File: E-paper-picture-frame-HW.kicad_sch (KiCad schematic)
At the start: 0 parts

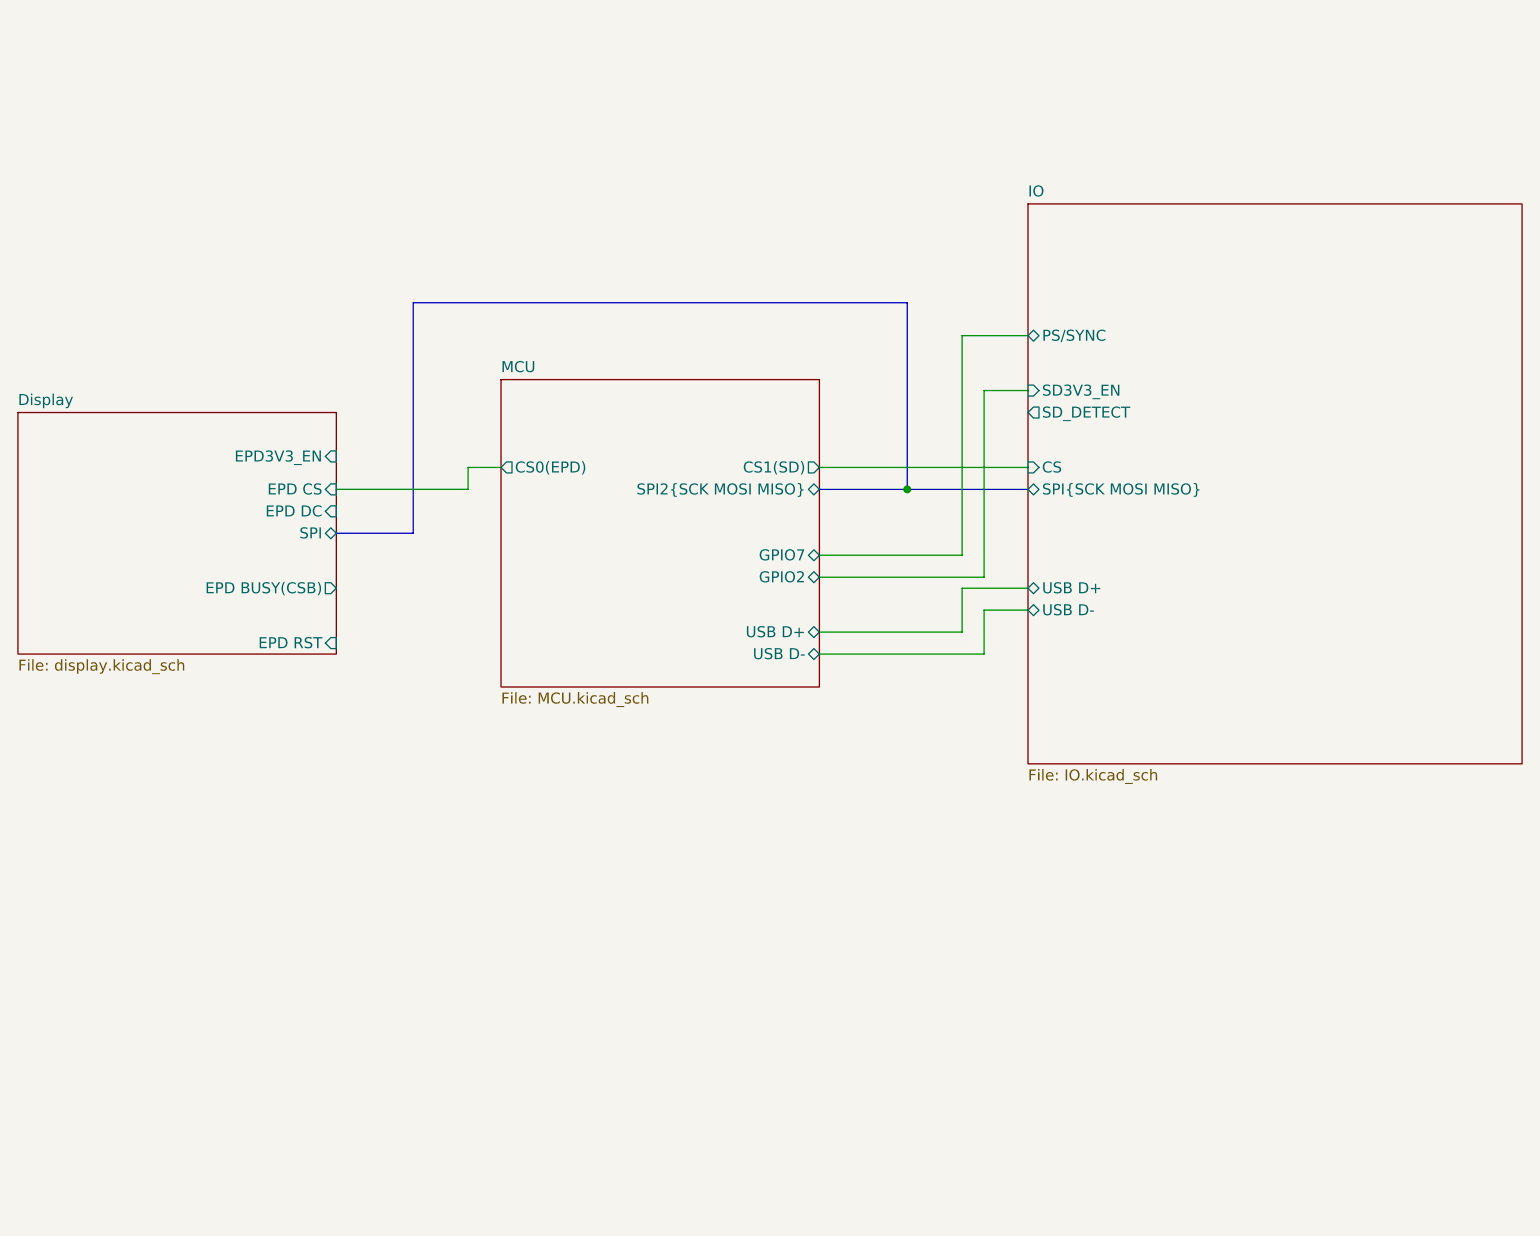
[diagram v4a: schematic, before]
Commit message: Final touches on schematic: Added test points Added LED Fixed symbol footprints
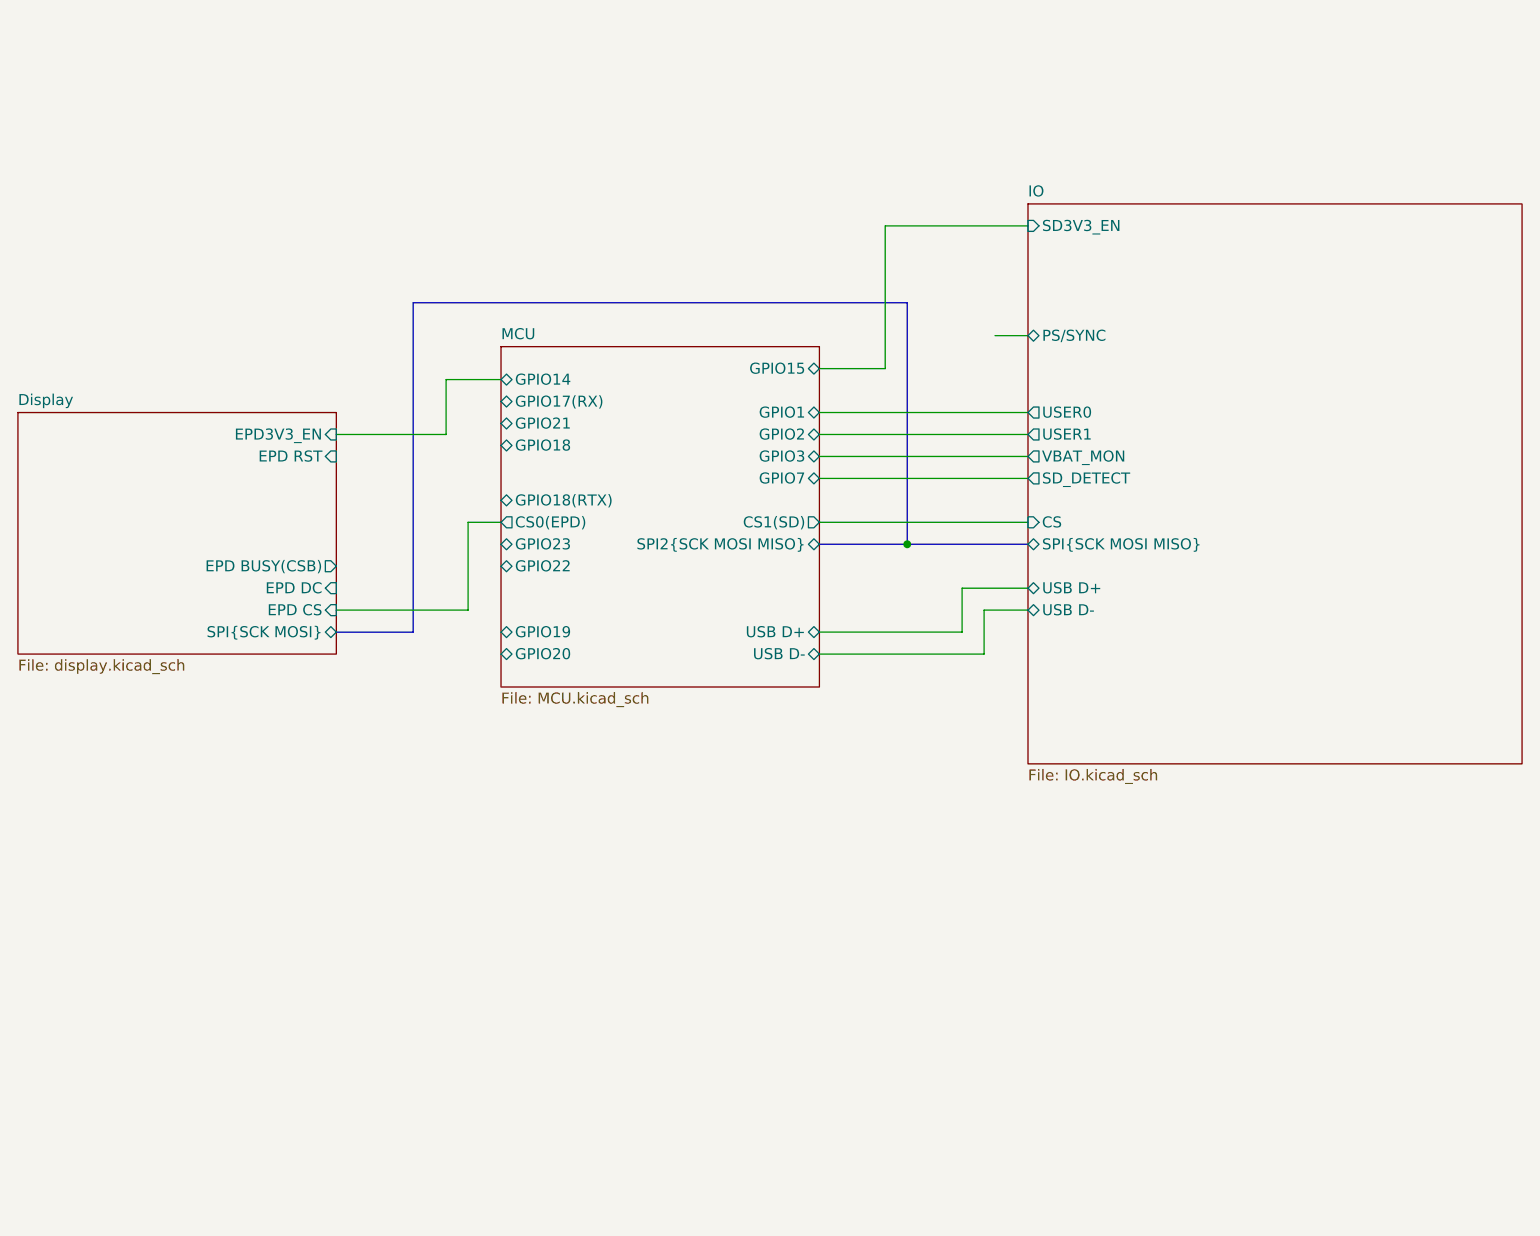
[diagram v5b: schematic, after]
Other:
- sheet Display ports: added SPI{SCK MOSI}; removed SPI
- sheet IO ports: added USER0, USER1, VBAT_MON; removed none
- sheet MCU ports: added GPIO1, GPIO14, GPIO15, GPIO17(RX), GPIO18, GPIO18(RTX), GPIO19, GPIO20, GPIO21, GPIO22, GPIO23, GPIO3; removed none

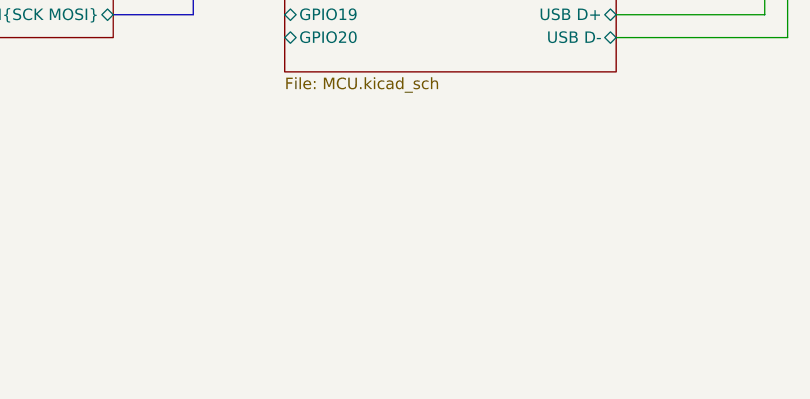
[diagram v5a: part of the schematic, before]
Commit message: Schematic cleanup and initial layout complete
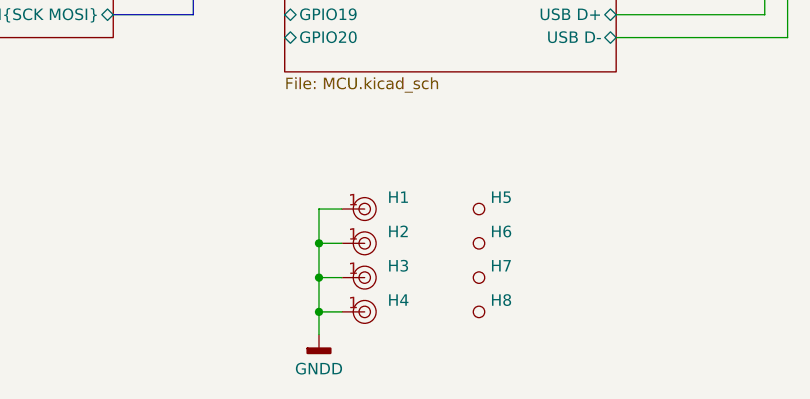
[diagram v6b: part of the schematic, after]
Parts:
- added H1, H2, H3, H4: ~, PCM_JLCPCB:Hole, 3mm, symbol PCM_JLCPCB-Manufacturing:Mounting Hole, 3mm, Via Stiched
- added H5, H6, H7, H8: ~, PCM_JLCPCB:Hole_Tooling_JLCPCB, symbol PCM_JLCPCB-Manufacturing:Tooling Hole, PCM_JLCPCB, 1.152mm
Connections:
- new net GNDD: H1.1, H2.1, H3.1, H4.1
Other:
- company: (none) -> Josef
- title: (none) -> E-paper frame Top level

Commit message: Small cleanup + linked jlcpcb parts for ordering
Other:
- note added: "Mounting/tooling holes"
